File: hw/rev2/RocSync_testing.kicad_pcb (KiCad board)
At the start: 2 copper layers, 250 x 250 mm, 336 parts, among them J1 USB_C_Receptacle_PowerOnly_6P, J2 BATT, J3 Conn_01x03_Pin, J4 Conn_01x04_Socket, SW1 ON/OFF, SW2 RESET, SW3 SW_Push, SW4 SW_Push, SW5 SW_Push, SW6 SW_Push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

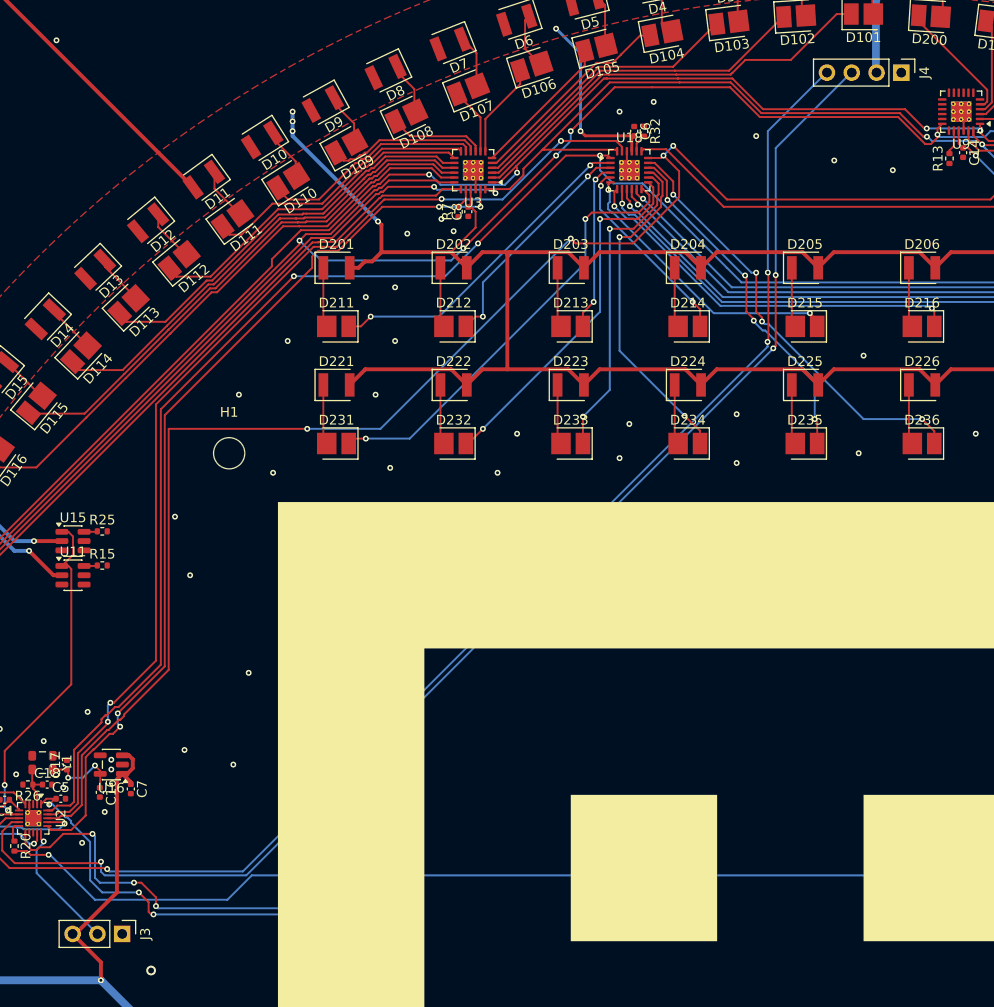
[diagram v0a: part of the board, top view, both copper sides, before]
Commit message: [hw] move headers to back layer to fix 3D render
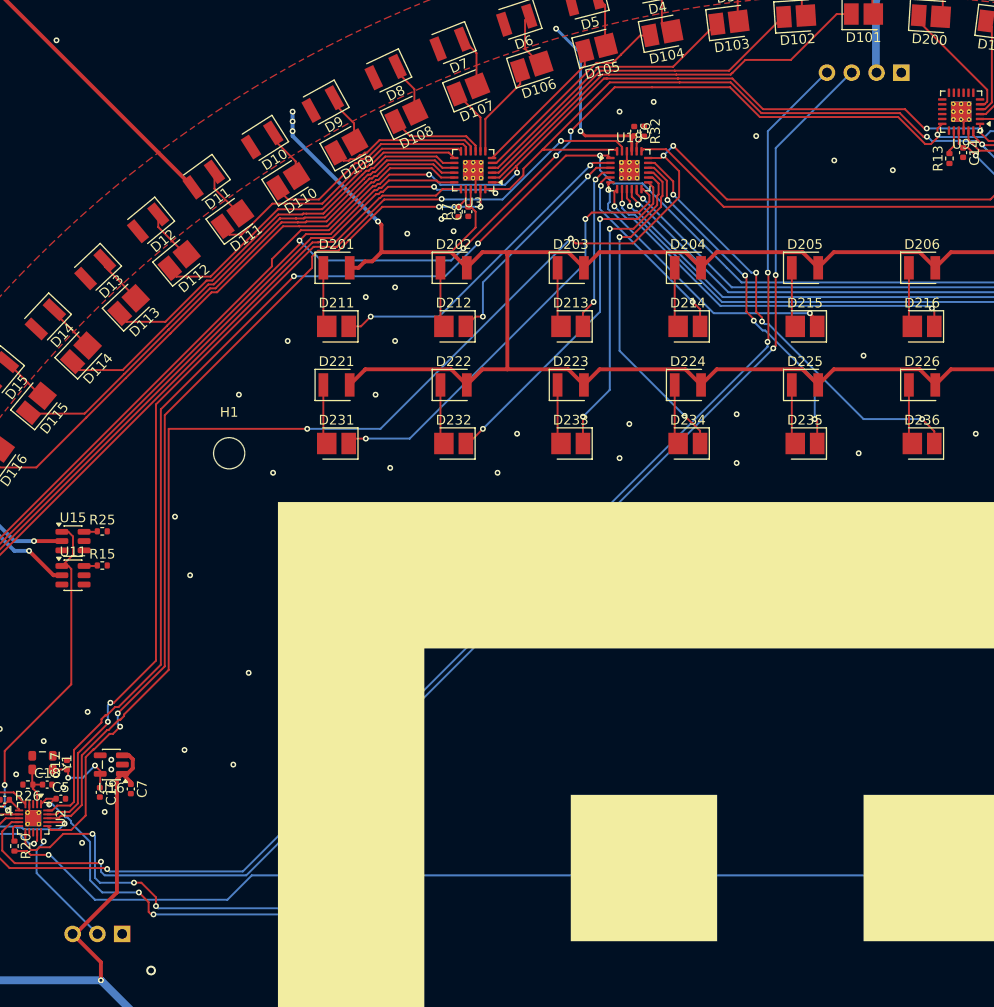
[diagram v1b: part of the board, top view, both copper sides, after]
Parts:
- J3, J4: moved to B.Cu
- turned J3 to 90 degrees
- turned J4 to 90 degrees
